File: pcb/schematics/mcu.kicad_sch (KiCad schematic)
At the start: 17 parts, among them SW2 Reset, U3 STM32F103V8Tx, Y2 24MHz

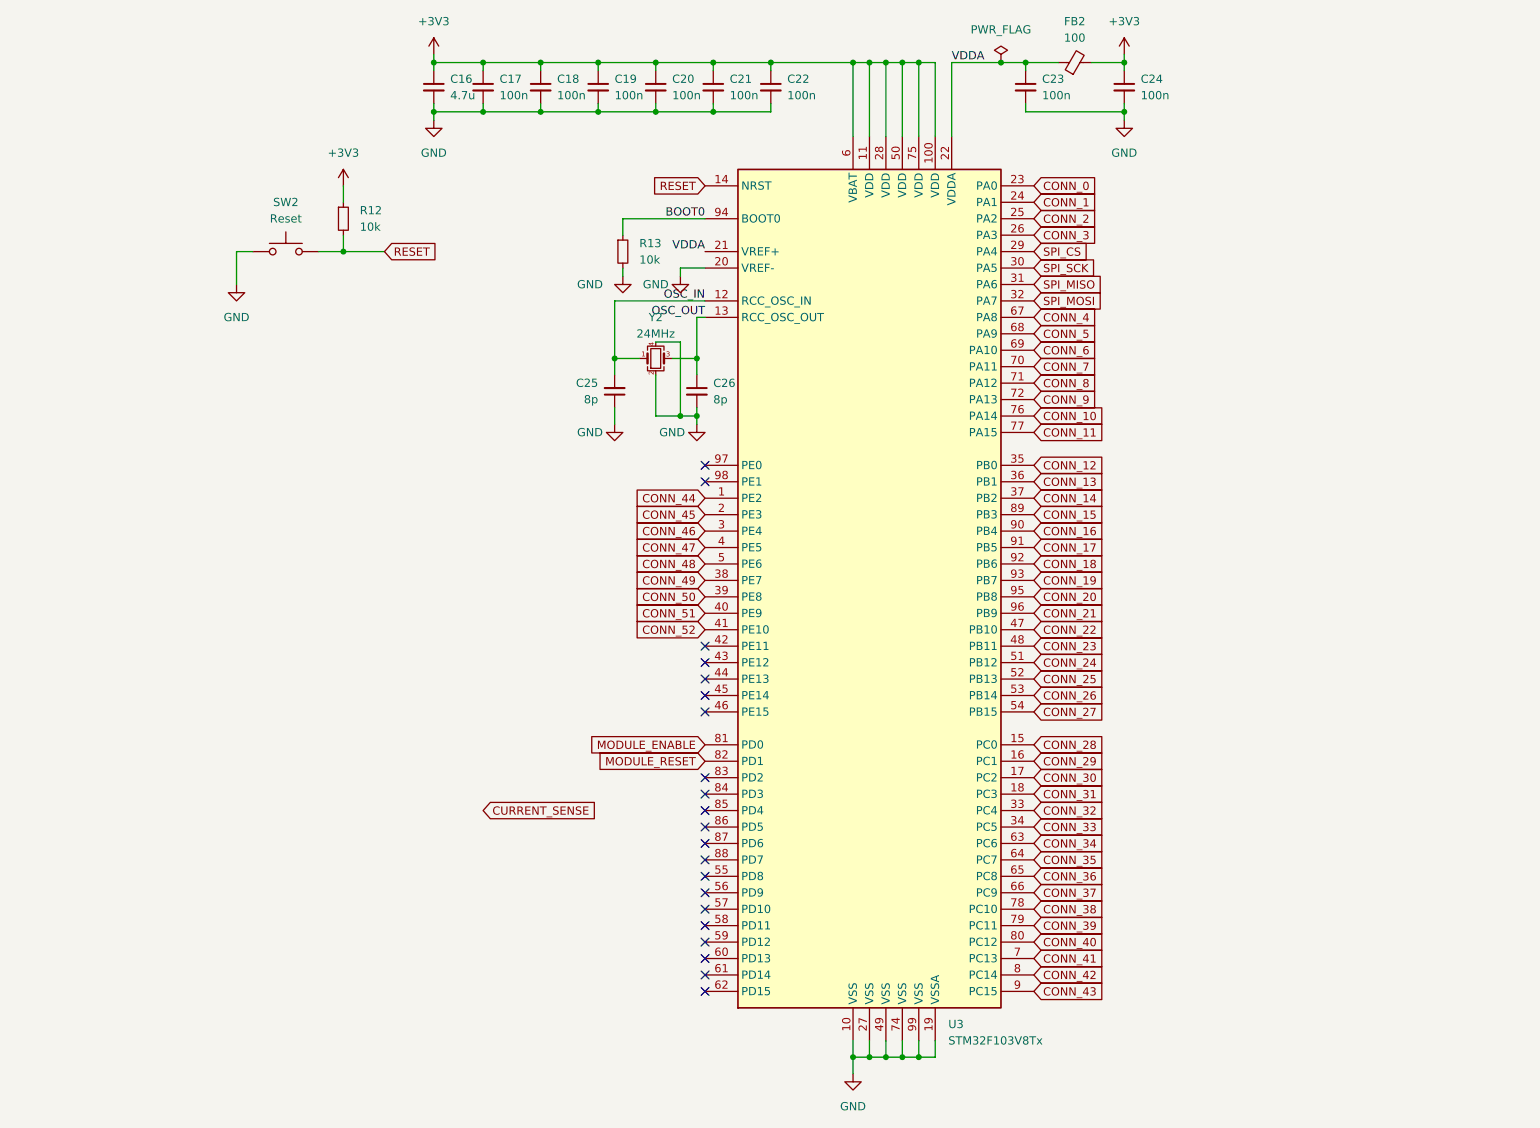
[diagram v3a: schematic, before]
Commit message: add SWD
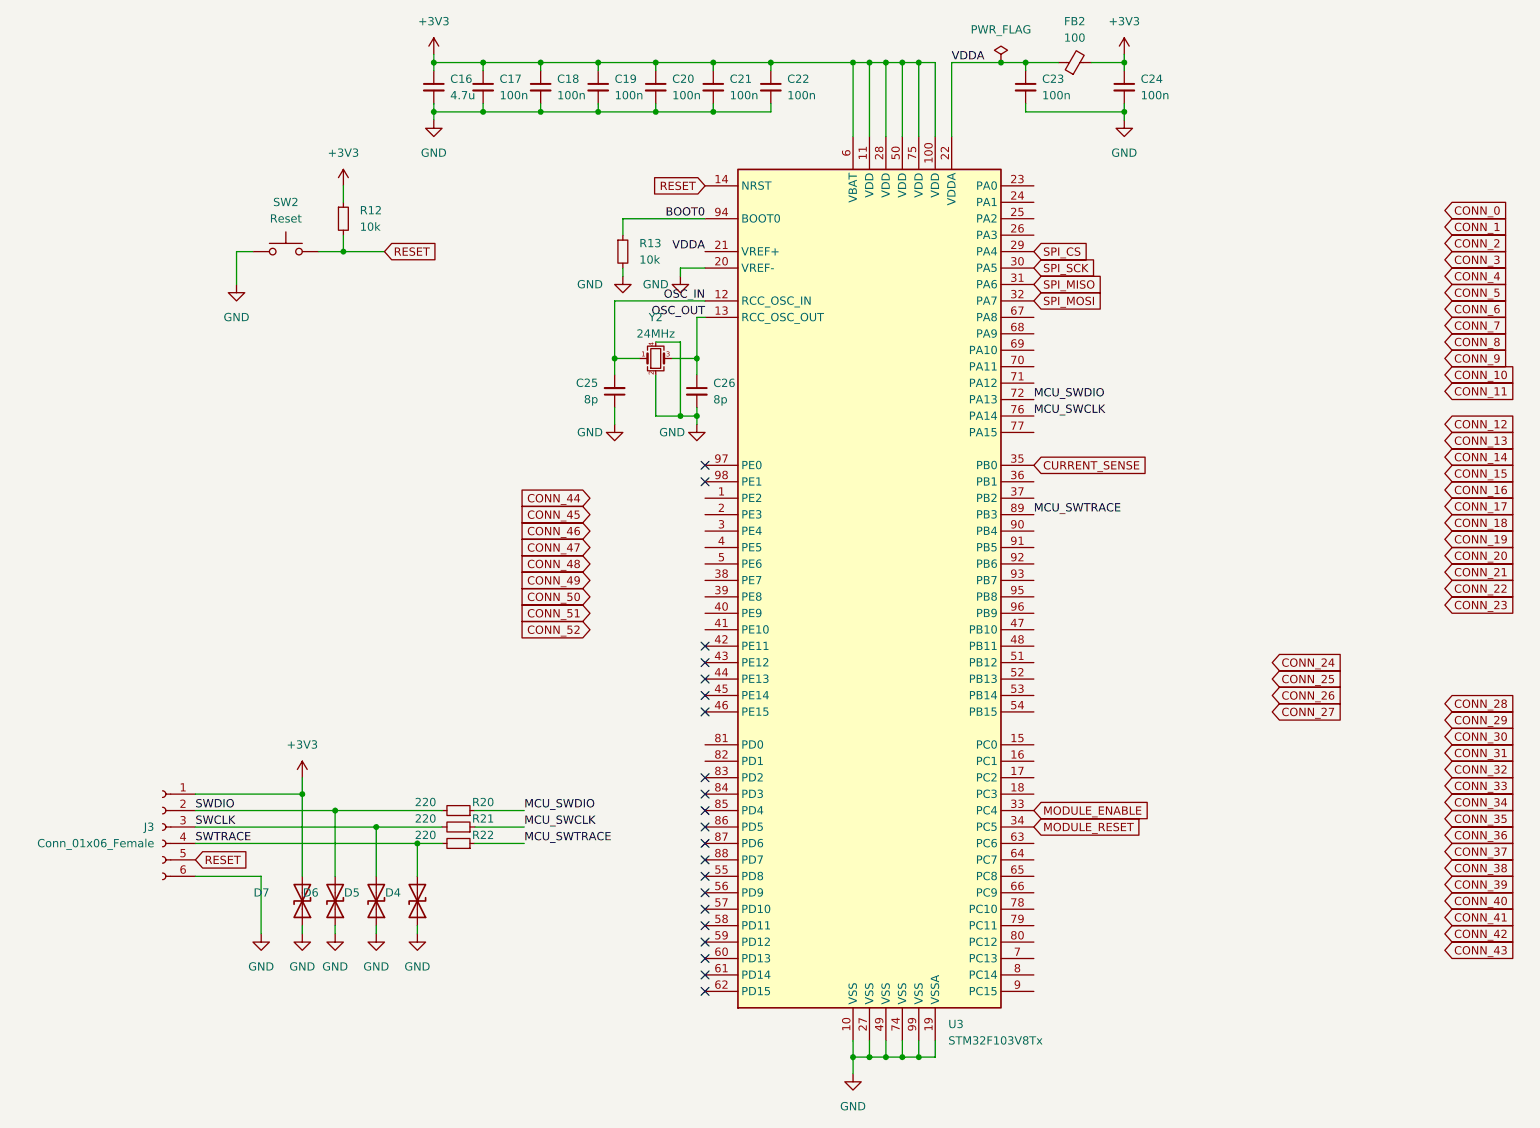
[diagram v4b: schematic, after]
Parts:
- added D4, D5, D6, D7: D_TVS, SOD-923-2:TVS_ESD9D5.0ST5G, symbol Device:D_TVS
- added J3: Conn_01x06_Female, Connector_PinHeader_1.27mm:PinHeader_1x06_P1.27mm_Vertical, symbol Connector:Conn_01x06_Female
- added R20, R21, R22: 220, Resistor_SMD:R_0603_1608Metric, symbol Device:R_Small
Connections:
- net +3V3: now also D7.2 (A2), J3.1 (Pin_1)
- net CONN_0: no longer U3.23 (PA0)
- net CONN_1: no longer U3.24 (PA1)
- net CONN_10: no longer U3.76 (PA14)
- net CONN_11: no longer U3.77 (PA15)
- net CONN_12: no longer U3.35 (PB0)
- net CONN_13: no longer U3.36 (PB1)
- net CONN_14: no longer U3.37 (PB2)
- net CONN_15: no longer U3.89 (PB3)
- net CONN_16: no longer U3.90 (PB4)
- net CONN_17: no longer U3.91 (PB5)
- net CONN_18: no longer U3.92 (PB6)
- net CONN_19: no longer U3.93 (PB7)
- net CONN_2: no longer U3.25 (PA2)
- net CONN_20: no longer U3.95 (PB8)
- net CONN_21: no longer U3.96 (PB9)
- net CONN_22: no longer U3.47 (PB10)
- net CONN_23: no longer U3.48 (PB11)
- net CONN_24: no longer U3.51 (PB12)
- net CONN_25: no longer U3.52 (PB13)
- net CONN_26: no longer U3.53 (PB14)
- net CONN_27: no longer U3.54 (PB15)
- net CONN_28: no longer U3.15 (PC0)
- net CONN_29: no longer U3.16 (PC1)
- net CONN_3: no longer U3.26 (PA3)
- net CONN_30: no longer U3.17 (PC2)
- net CONN_31: no longer U3.18 (PC3)
- net CONN_32: no longer U3.33 (PC4)
- net CONN_33: no longer U3.34 (PC5)
- net CONN_34: no longer U3.63 (PC6)
- net CONN_35: no longer U3.64 (PC7)
- net CONN_36: no longer U3.65 (PC8)
- net CONN_37: no longer U3.66 (PC9)
- net CONN_38: no longer U3.78 (PC10)
- net CONN_39: no longer U3.79 (PC11)
- net CONN_4: no longer U3.67 (PA8)
- net CONN_40: no longer U3.80 (PC12)
- net CONN_41: no longer U3.7 (PC13)
- net CONN_42: no longer U3.8 (PC14)
- net CONN_43: no longer U3.9 (PC15)
- net CONN_44: no longer U3.1 (PE2)
- net CONN_45: no longer U3.2 (PE3)
- net CONN_46: no longer U3.3 (PE4)
- net CONN_47: no longer U3.4 (PE5)
- net CONN_48: no longer U3.5 (PE6)
- net CONN_49: no longer U3.38 (PE7)
- net CONN_5: no longer U3.68 (PA9)
- net CONN_50: no longer U3.39 (PE8)
- net CONN_51: no longer U3.40 (PE9)
- net CONN_52: no longer U3.41 (PE10)
- net CONN_6: no longer U3.69 (PA10)
- net CONN_7: no longer U3.70 (PA11)
- net CONN_8: no longer U3.71 (PA12)
- net CONN_9: no longer U3.72 (PA13)
- net CURRENT_SENSE: now also U3.35 (PB0)
- net GND: now also D4.1 (A1), D5.1 (A1), D6.1 (A1), D7.1 (A1), J3.6 (Pin_6)
- net MODULE_ENABLE: now also U3.33 (PC4); no longer U3.81 (PD0)
- net MODULE_RESET: now also U3.34 (PC5); no longer U3.82 (PD1)
- net RESET: now also J3.5 (Pin_5)
- new net MCU_SWCLK: R21.1, U3.76 (PA14)
- new net MCU_SWDIO: R20.1, U3.72 (PA13)
- new net MCU_SWTRACE: R22.1, U3.89 (PB3)
- new net SWCLK: D5.2 (A2), J3.3 (Pin_3), R21.2
- new net SWDIO: D6.2 (A2), J3.2 (Pin_2), R20.2
- new net SWTRACE: D4.2 (A2), J3.4 (Pin_4), R22.2

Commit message: add bus traces
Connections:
- net CONN_37: now also U3.85 (PD4)
- net CONN_38: now also U3.84 (PD3)
- net CONN_39: now also U3.83 (PD2)
- net CONN_40: now also U3.82 (PD1)
- net CONN_41: now also U3.81 (PD0)
- net CONN_42: now also U3.80 (PC12)
- net CONN_43: now also U3.79 (PC11)
- net CONN_44: now also U3.78 (PC10)
- net CONN_45: now also U3.77 (PA15)
- net CONN_46: now also U3.71 (PA12)
- net CONN_47: now also U3.70 (PA11)
- net CONN_48: now also U3.69 (PA10)
- net CONN_49: now also U3.68 (PA9)
- net CONN_50: now also U3.67 (PA8)
- net CONN_51: now also U3.66 (PC9)
- net CONN_52: now also U3.65 (PC8)
- no-connect marks 21 -> 7
